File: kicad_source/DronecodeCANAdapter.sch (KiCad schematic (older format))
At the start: 18 parts, among them CN1 CONN_01X05, CN2 691322310004, CN3 GH_SM04B-GHS-TB, CN4 GH_SM04B-GHS-TB, U1 TCAN332GDR

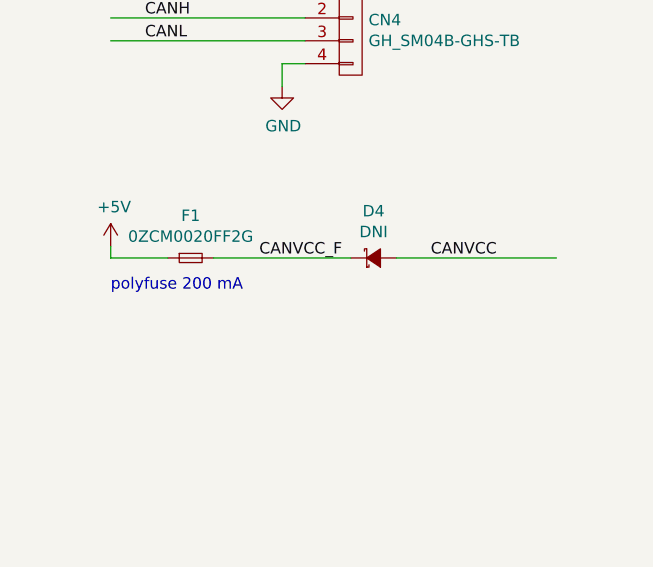
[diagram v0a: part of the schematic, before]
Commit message: corrected footprint of CAN transceiver
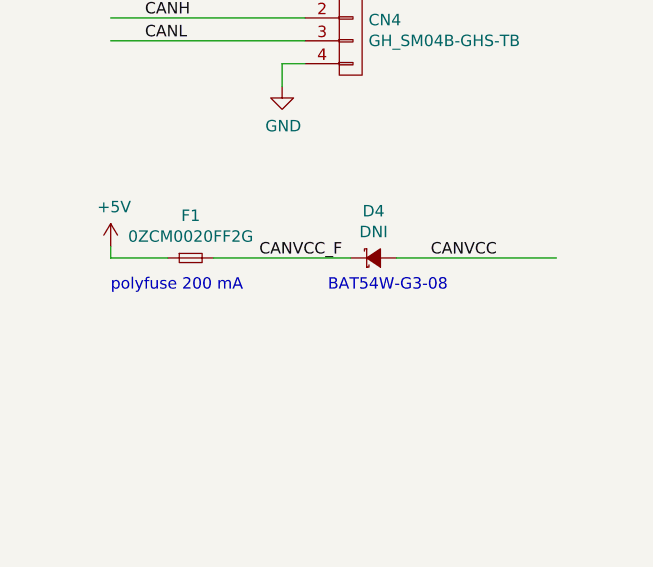
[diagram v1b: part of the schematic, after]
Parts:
- U1: footprint SOIC:SOIJ-8_5.3x5.3mm_Pitch1.27mm -> SOIC:SOIC-8_3.9x4.9mm_Pitch1.27mm
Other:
- note added: "BAT54W-G3-08"
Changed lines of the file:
@@
 Sheet 1 1
 Title "DronecodeCANAdapter"
-Date "2021-01-02"
-Rev "0.1"
+Date "2021-01-25"
+Rev "0.2"
 Comp "generationmake"
 Comment1 ""
@@
 F 0 "U1" H 4775 2887 60  0000 C CNN
 F 1 "TCAN332GDR" H 4775 2781 60  0000 C CNN
-F 2 "SOIC:SOIJ-8_5.3x5.3mm_Pitch1.27mm" H 5100 1950 60  0001 C CNN
+F 2 "SOIC:SOIC-8_3.9x4.9mm_Pitch1.27mm" H 5100 1950 60  0001 C CNN
 F 3 "" H 4250 2150 60  0000 C CNN
 	1    4250 2000
@@
 $EndComp
 NoConn ~ 5750 5700
+Text Notes 10000 3550 0    50   ~ 0
+ BAT54W-G3-08
 $EndSCHEMATC

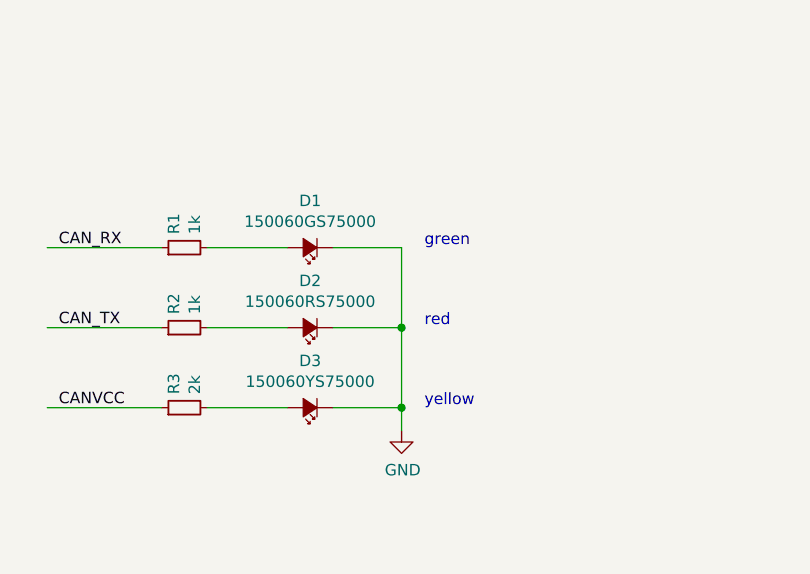
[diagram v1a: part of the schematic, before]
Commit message: made debug leds low active
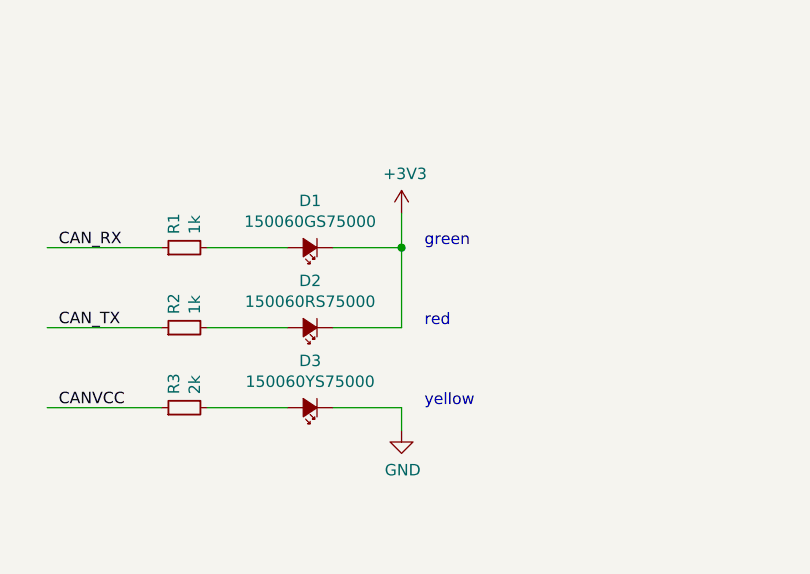
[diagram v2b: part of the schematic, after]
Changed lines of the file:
@@
 Sheet 1 1
 Title "DronecodeCANAdapter"
-Date "2021-01-25"
+Date "2021-01-26"
 Rev "0.2"
 Comp "generationmake"
@@
 Wire Wire Line
 	6300 3650 6600 3650
-Connection ~ 6600 3650
-Wire Wire Line
-	6600 3650 6600 4000
 Wire Wire Line
 	6300 4000 6600 4000
-Connection ~ 6600 4000
 Wire Wire Line
 	6600 4000 6600 4100
@@
 Text Notes 10000 3550 0    50   ~ 0
  BAT54W-G3-08
+$Comp
+L power-supply:+3V3 #PWR?
+U 1 1 600F7B1B
+P 6600 3150
+AR Path="/5FD58A5B/600F7B1B" Ref="#PWR?"  Part="1"
+AR Path="/600F7B1B" Ref="#PWR0101"  Part="1"
+F 0 "#PWR0101" H 6600 3000 50  0001 C CNN
+F 1 "+3V3" H 6615 3323 50  0000 C CNN
+F 2 "" H 6600 3150 50  0000 C CNN
+F 3 "" H 6600 3150 50  0000 C CNN
+	1    6600 3150
+	1    0    0    -1
+$EndComp
+Wire Wire Line
+	6600 3300 6600 3150
+Connection ~ 6600 3300
 $EndSCHEMATC

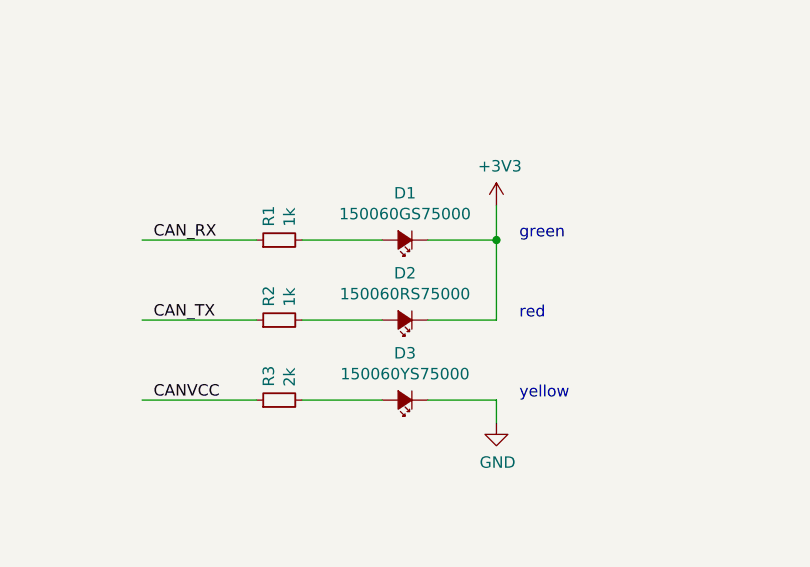
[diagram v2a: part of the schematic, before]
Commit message: corrected polarity of leds
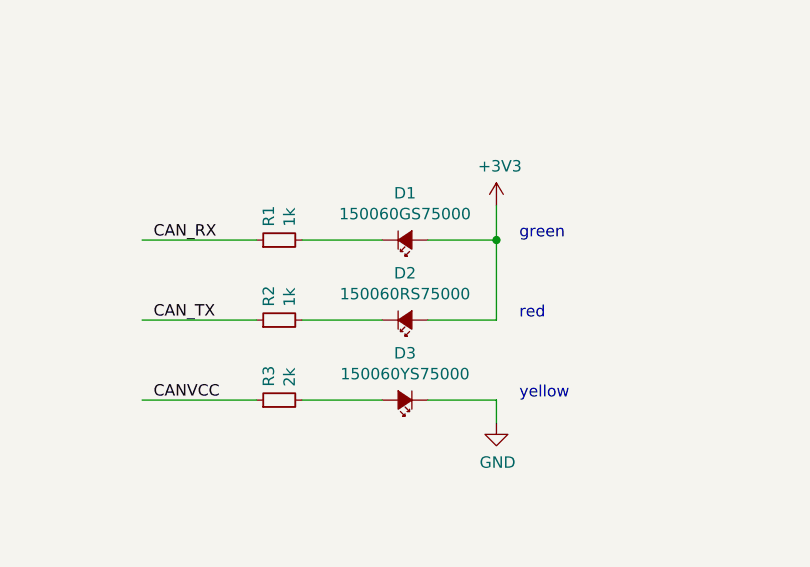
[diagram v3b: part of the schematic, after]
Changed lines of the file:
@@
 F 3 "" V 6200 3300 50  0000 C CNN
 	1    6200 3300
-	-1   0    0    1
+	1    0    0    1
 $EndComp
 $Comp
@@
 F 3 "" V 6200 3650 50  0000 C CNN
 	1    6200 3650
-	-1   0    0    1
+	1    0    0    1
 $EndComp
 $Comp
